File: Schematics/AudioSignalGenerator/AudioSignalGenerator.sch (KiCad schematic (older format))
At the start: 6 parts, among them J1 Conn_01x02_Male, SW1 SW_SPST, SW2 SW_SPST, U1 OLED_1DOT3, U2 PCM5102_MODULE

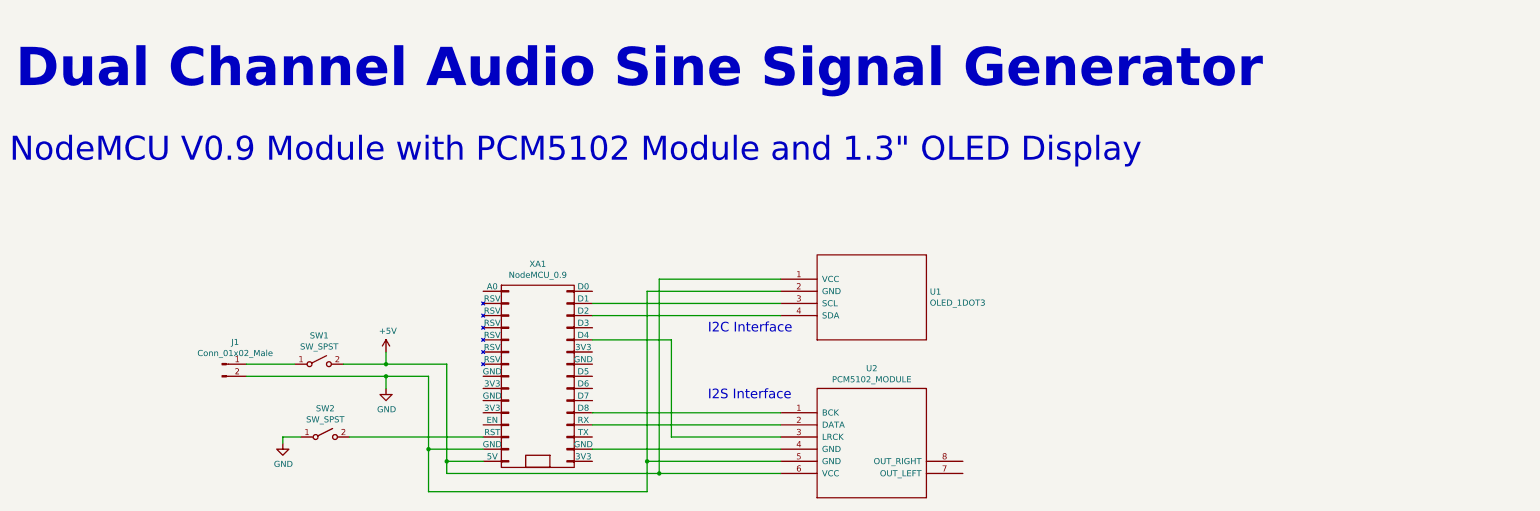
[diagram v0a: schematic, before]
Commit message: changed schematics, added documentation (TeX)
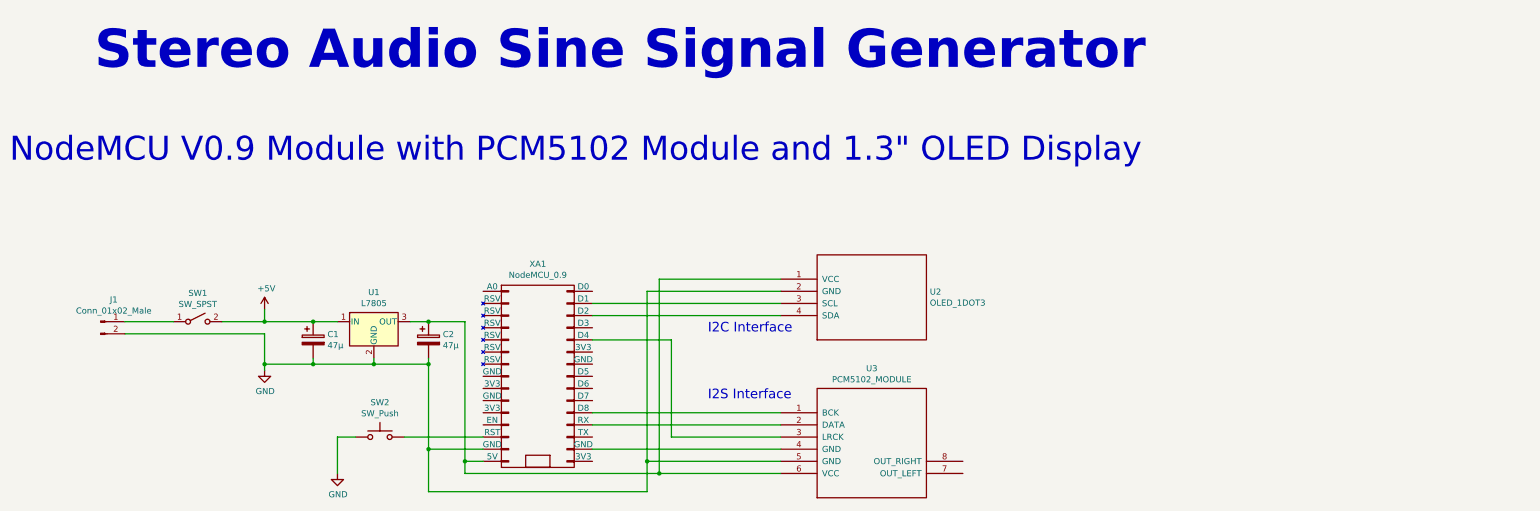
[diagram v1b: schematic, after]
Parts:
- removed SW2: SW_SPST, symbol Switch:SW_SPST
- added C1, C2: 47µ, symbol Device:CP
- added SW2: SW_Push, symbol Switch:SW_Push
- added U1: L7805, symbol Regulator_Linear:L7805
- renumbered U1 to U2, U2 to U3
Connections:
- net +5V: now also C1.1, U1.1 (IN); no longer U2.1 (VCC), U3.6 (VCC), XA1.15 (5V)
- net GND: now also C1.2, C2.2, SW2.1, U1.2 (GND)
- net at XA1.13 (RST): now also SW2.2
- new net: C2.1, U1.3 (OUT), U2.1 (VCC), U3.6 (VCC), XA1.15 (5V)
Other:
- note added: "Stereo Audio Sine Signal Generator"
- note removed: "Dual Channel Audio Sine Signal Generator"
- moved on the sheet: J1, SW1
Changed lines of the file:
@@
 L Connector:Conn_01x02_Male J1
 U 1 1 601EBB44
-P 2450 3650
-F 0 "J1" H 2558 3831 50  0000 C CNN
-F 1 "Conn_01x02_Male" H 2558 3740 50  0000 C CNN
-F 2 "" H 2450 3650 50  0001 C CNN
-F 3 "~" H 2450 3650 50  0001 C CNN
-	1    2450 3650
+P 1450 3300
+F 0 "J1" H 1558 3481 50  0000 C CNN
+F 1 "Conn_01x02_Male" H 1558 3390 50  0000 C CNN
+F 2 "" H 1450 3300 50  0001 C CNN
+F 3 "~" H 1450 3300 50  0001 C CNN
+	1    1450 3300
 	1    0    0    -1
 $EndComp
@@
 L power:+5V #PWR01
 U 1 1 601EBF63
-P 3800 3550
-F 0 "#PWR01" H 3800 3400 50  0001 C CNN
-F 1 "+5V" H 3815 3723 50  0000 C CNN
-F 2 "" H 3800 3550 50  0001 C CNN
-F 3 "" H 3800 3550 50  0001 C CNN
-	1    3800 3550
+P 2800 3200
+F 0 "#PWR01" H 2800 3050 50  0001 C CNN
+F 1 "+5V" H 2815 3373 50  0000 C CNN
+F 2 "" H 2800 3200 50  0001 C CNN
+F 3 "" H 2800 3200 50  0001 C CNN
+	1    2800 3200
 	1    0    0    -1
 $EndComp
@@
 L power:GND #PWR02
 U 1 1 601EC43C
-P 3800 3850
-F 0 "#PWR02" H 3800 3600 50  0001 C CNN
-F 1 "GND" H 3805 3677 50  0000 C CNN
-F 2 "" H 3800 3850 50  0001 C CNN
-F 3 "" H 3800 3850 50  0001 C CNN
-	1    3800 3850
+P 2800 3700
+F 0 "#PWR02" H 2800 3450 50  0001 C CNN
+F 1 "GND" H 2805 3527 50  0000 C CNN
+F 2 "" H 2800 3700 50  0001 C CNN
+F 3 "" H 2800 3700 50  0001 C CNN
+	1    2800 3700
 	1    0    0    -1
 $EndComp
@@
 	1    0    0    -1
 $EndComp
-Text Notes 750  1400 0    315  ~ 63
-Dual Channel Audio Sine Signal Generator
-$Comp
-L OLED_1DOT3:OLED_1DOT3 U1
+Text Notes 1400 1250 0    315  ~ 63
+Stereo Audio Sine Signal Generator
+$Comp
+L OLED_1DOT3:OLED_1DOT3 U2
 U 1 1 601F4A30
 P 7800 3100
-F 0 "U1" H 8278 3146 50  0000 L CNN
+F 0 "U2" H 8278 3146 50  0000 L CNN
 F 1 "OLED_1DOT3" H 8278 3055 50  0000 L CNN
 F 2 "MODULE" H 7800 3100 50  0001 C CNN
@@
 $EndComp
 $Comp
-L PCM5102_MODULE:PCM5102_MODULE U2
+L PCM5102_MODULE:PCM5102_MODULE U3
 U 1 1 601F5253
 P 7800 4300
-F 0 "U2" H 7800 4915 50  0000 C CNN
+F 0 "U3" H 7800 4915 50  0000 C CNN
 F 1 "PCM5102_MODULE" H 7800 4824 50  0000 C CNN
 F 2 "MODULE" H 7800 4300 50  0001 C CNN
@@
 $EndComp
 Wire Wire Line
-	3800 3650 3800 3550
-Wire Wire Line
-	3800 3750 3800 3850
-Wire Wire Line
-	3800 3750 4150 3750
-Wire Wire Line
-	4150 3750 4150 4350
+	2800 3300 2800 3200
+Wire Wire Line
+	2800 3400 2800 3650
+Wire Wire Line
+	4150 3650 4150 4350
 Wire Wire Line
 	4150 4350 4600 4350
-Connection ~ 3800 3750
-Wire Wire Line
-	4600 4450 4300 4450
-Wire Wire Line
-	4300 4450 4300 3650
-Wire Wire Line
-	4300 3650 3800 3650
-Connection ~ 3800 3650
+Wire Wire Line
+	4600 4450 4450 4450
+Wire Wire Line
+	3200 3300 2800 3300
+Connection ~ 2800 3300
 Wire Wire Line
 	5500 4350 7050 4350
@@
 Connection ~ 4150 4350
 Wire Wire Line
-	4300 4450 4300 4550
-Connection ~ 4300 4450
-Wire Wire Line
-	4300 4550 6050 4550
+	4450 4450 4450 4550
+Connection ~ 4450 4450
+Wire Wire Line
+	4450 4550 6050 4550
 Wire Wire Line
 	6050 4550 6050 2950
@@
 L Switch:SW_SPST SW1
 U 1 1 6021EC58
-P 3250 3650
-F 0 "SW1" H 3250 3885 50  0000 C CNN
-F 1 "SW_SPST" H 3250 3794 50  0000 C CNN
-F 2 "" H 3250 3650 50  0001 C CNN
-F 3 "~" H 3250 3650 50  0001 C CNN
-	1    3250 3650
-	1    0    0    -1
-$EndComp
-Wire Wire Line
-	2650 3750 3800 3750
-Wire Wire Line
-	2650 3650 3050 3650
-Wire Wire Line
-	3450 3650 3800 3650
-$Comp
-L Switch:SW_SPST SW2
-U 1 1 60221C7B
-P 3300 4250
-F 0 "SW2" H 3300 4485 50  0000 C CNN
-F 1 "SW_SPST" H 3300 4394 50  0000 C CNN
-F 2 "" H 3300 4250 50  0001 C CNN
-F 3 "~" H 3300 4250 50  0001 C CNN
-	1    3300 4250
-	1    0    0    -1
-$EndComp
+P 2250 3300
+F 0 "SW1" H 2250 3535 50  0000 C CNN
+F 1 "SW_SPST" H 2250 3444 50  0000 C CNN
+F 2 "" H 2250 3300 50  0001 C CNN
+F 3 "~" H 2250 3300 50  0001 C CNN
+	1    2250 3300
+	1    0    0    -1
+$EndComp
+Wire Wire Line
+	1650 3400 2800 3400
+Wire Wire Line
+	1650 3300 2050 3300
+Wire Wire Line
+	2450 3300 2800 3300
 $Comp
 L power:GND #PWR03
 U 1 1 602220C7
-P 2950 4300
-F 0 "#PWR03" H 2950 4050 50  0001 C CNN
-F 1 "GND" H 2955 4127 50  0000 C CNN
-F 2 "" H 2950 4300 50  0001 C CNN
-F 3 "" H 2950 4300 50  0001 C CNN
-	1    2950 4300
-	1    0    0    -1
-$EndComp
-Wire Wire Line
-	3100 4250 2950 4250
-Wire Wire Line
-	2950 4250 2950 4300
-Wire Wire Line
-	3500 4250 4600 4250
+P 3400 4550
+F 0 "#PWR03" H 3400 4300 50  0001 C CNN
+F 1 "GND" H 3405 4377 50  0000 C CNN
+F 2 "" H 3400 4550 50  0001 C CNN
+F 3 "" H 3400 4550 50  0001 C CNN
+	1    3400 4550
+	1    0    0    -1
+$EndComp
+Wire Wire Line
+	3400 4250 3400 4550
+$Comp
+L Regulator_Linear:L7805 U1
+U 1 1 6022FD46
+P 3700 3300
+F 0 "U1" H 3700 3542 50  0000 C CNN
+F 1 "L7805" H 3700 3451 50  0000 C CNN
+F 2 "" H 3725 3150 50  0001 L CIN
+F 3 "http://www.st.com/content/ccc/resource/technical/document/datasheet/41/4f/b3/b0/12/d4/47/88/CD00000444.pdf/files/CD00000444.pdf/jcr:content/translations/en.CD00000444.pdf" H 3700 3250 50  0001 C CNN
+	1    3700 3300
+	1    0    0    -1
+$EndComp
+$Comp
+L Device:CP C1
+U 1 1 6023D1A5
+P 3200 3450
+F 0 "C1" H 3318 3496 50  0000 L CNN
+F 1 "47µ" H 3318 3405 50  0000 L CNN
+F 2 "" H 3238 3300 50  0001 C CNN
+F 3 "~" H 3200 3450 50  0001 C CNN
+	1    3200 3450
+	1    0    0    -1
+$EndComp
+$Comp
+L Device:CP C2
+U 1 1 6023D674
+P 4150 3450
+F 0 "C2" H 4268 3496 50  0000 L CNN
+F 1 "47µ" H 4268 3405 50  0000 L CNN
+F 2 "" H 4188 3300 50  0001 C CNN
+F 3 "~" H 4150 3450 50  0001 C CNN
+	1    4150 3450
+	1    0    0    -1
+$EndComp
+Wire Wire Line
+	3200 3650 2800 3650
+Connection ~ 3200 3650
+Wire Wire Line
+	3200 3650 3200 3600
+Connection ~ 2800 3650
+Wire Wire Line
+	2800 3650 2800 3700
+Wire Wire Line
+	3200 3650 3700 3650
+Wire Wire Line
+	3700 3650 3700 3600
+Wire Wire Line
+	3700 3650 4150 3650
+Wire Wire Line
+	4150 3650 4150 3600
+Connection ~ 3700 3650
+Connection ~ 4150 3650
+Wire Wire Line
+	4000 3300 4150 3300
+Wire Wire Line
+	4150 3300 4450 3300
+Wire Wire Line
+	4450 3300 4450 4450
+Connection ~ 4150 3300
+Wire Wire Line
+	3400 3300 3200 3300
+Connection ~ 3200 3300
+Wire Wire Line
+	3950 4250 4600 4250
+Wire Wire Line
+	3550 4250 3400 4250
+$Comp
+L Switch:SW_Push SW2
+U 1 1 6022BD42
+P 3750 4250
+F 0 "SW2" H 3750 4535 50  0000 C CNN
+F 1 "SW_Push" H 3750 4444 50  0000 C CNN
+F 2 "" H 3750 4450 50  0001 C CNN
+F 3 "~" H 3750 4450 50  0001 C CNN
+	1    3750 4250
+	1    0    0    -1
+$EndComp
 $EndSCHEMATC
